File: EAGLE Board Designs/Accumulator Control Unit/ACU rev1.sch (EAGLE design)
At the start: 191 parts, among them J1 CONNECTOR-CAN_MF_T_V_, J2 CONNECTOR-8_MF_T_V_, J3 CONNECTOR-8_MF_T_V_, J4 CONNECTOR-2_MF_T_V_, J5 CONNECTOR-12_MF_T_V_, Q1 TRANSISTOR_N_MOS__PMV15ENEA, Q2 TRANSISTOR_N_MOS__PMV15ENEA, T1 TRANSFORMER_HM2112ZNLT_AIRGAP, U10 OPAMP_1_CHANNEL_OPA991, U11 LOGICGATE_AND_DCK3, U12 OPAMP_1_CHANNEL_OPA991, U13 OPAMP_1_CHANNEL_OPA991, U14 OPAMP_1_CHANNEL_OPA991, U15 LOGICGATE_AND_DCK3, U18 OPAMP_1_CHANNEL_OPA991, U19 MAX7404, U2 ADG1423, U20 OPAMP_1_CHANNEL_OPA991, U22 OPAMP_1_CHANNEL_OPA991, U25 TCAN1051HQV-Q1, U26 MAX7404, U27 OPAMP_1_CHANNEL_OPA991, U28 MAX7404, U29 OPAMP_1_CHANNEL_OPA991, U3 LM555, U30 MAX7404, U4 OPAMP_1_CHANNEL_OPA991, U5 LTC6820, U6 ADM823, U7 OPAMP_1_CHANNEL_OPA991, U8 LOGICGATE_AND_DCK3, U9 OPAMP_1_CHANNEL_OPA991

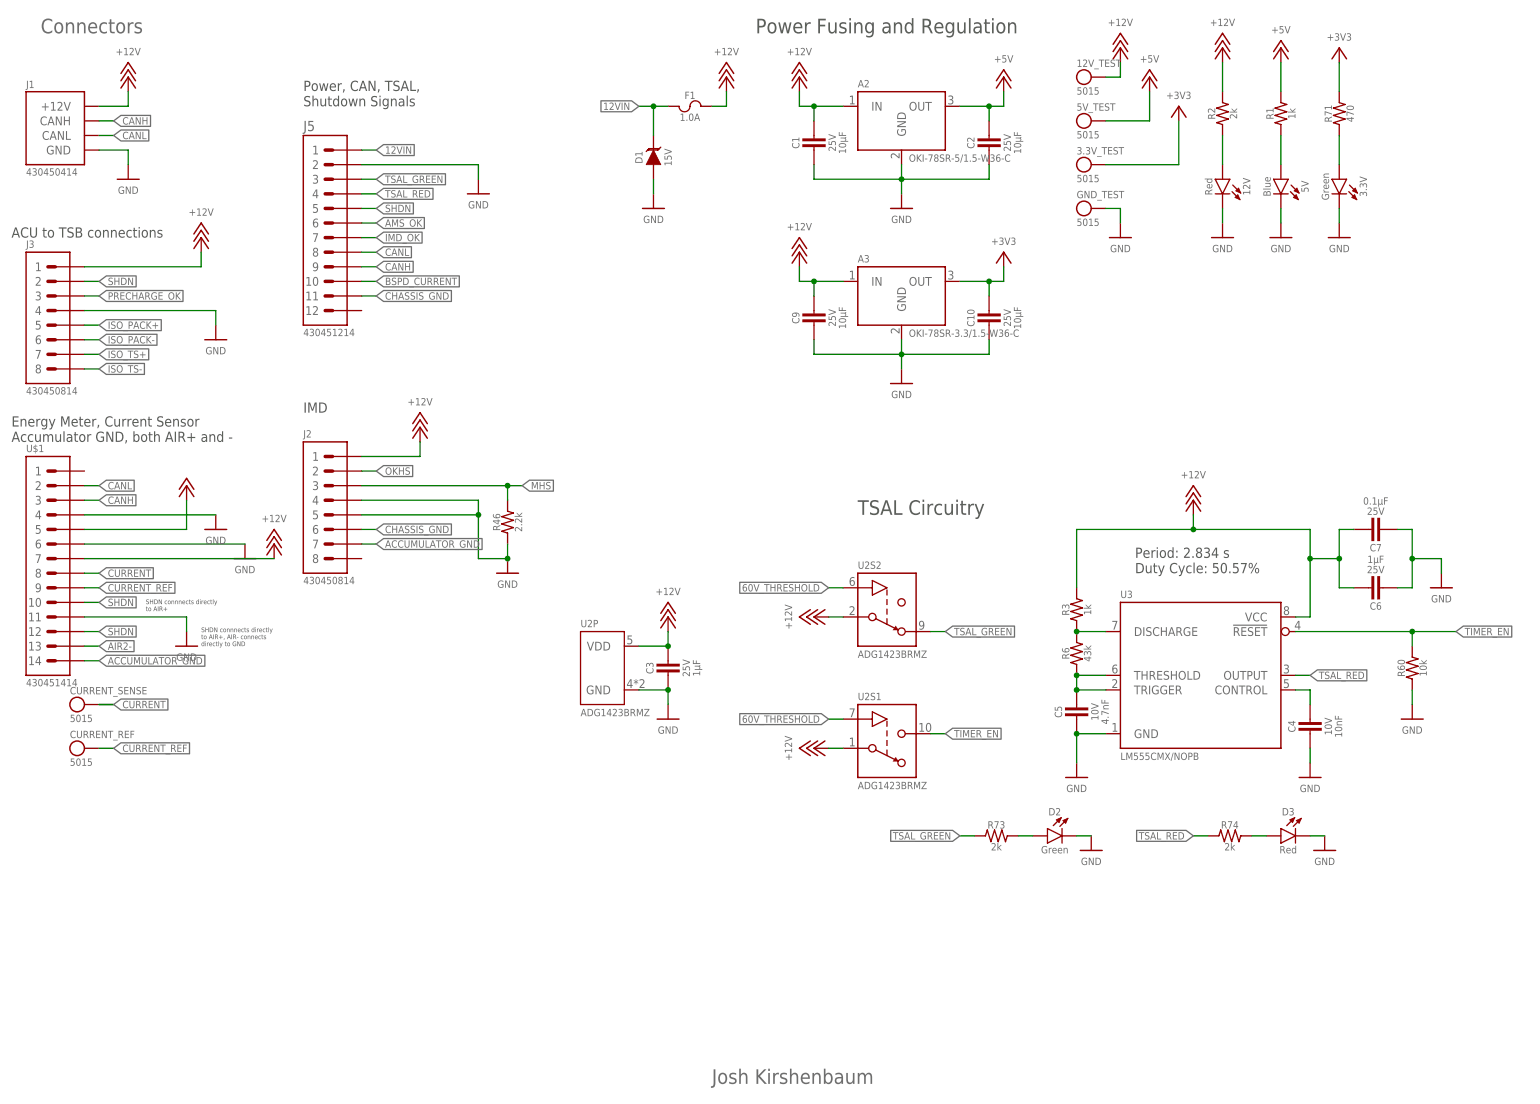
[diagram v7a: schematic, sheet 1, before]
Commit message: fix hole spacing and add some leds
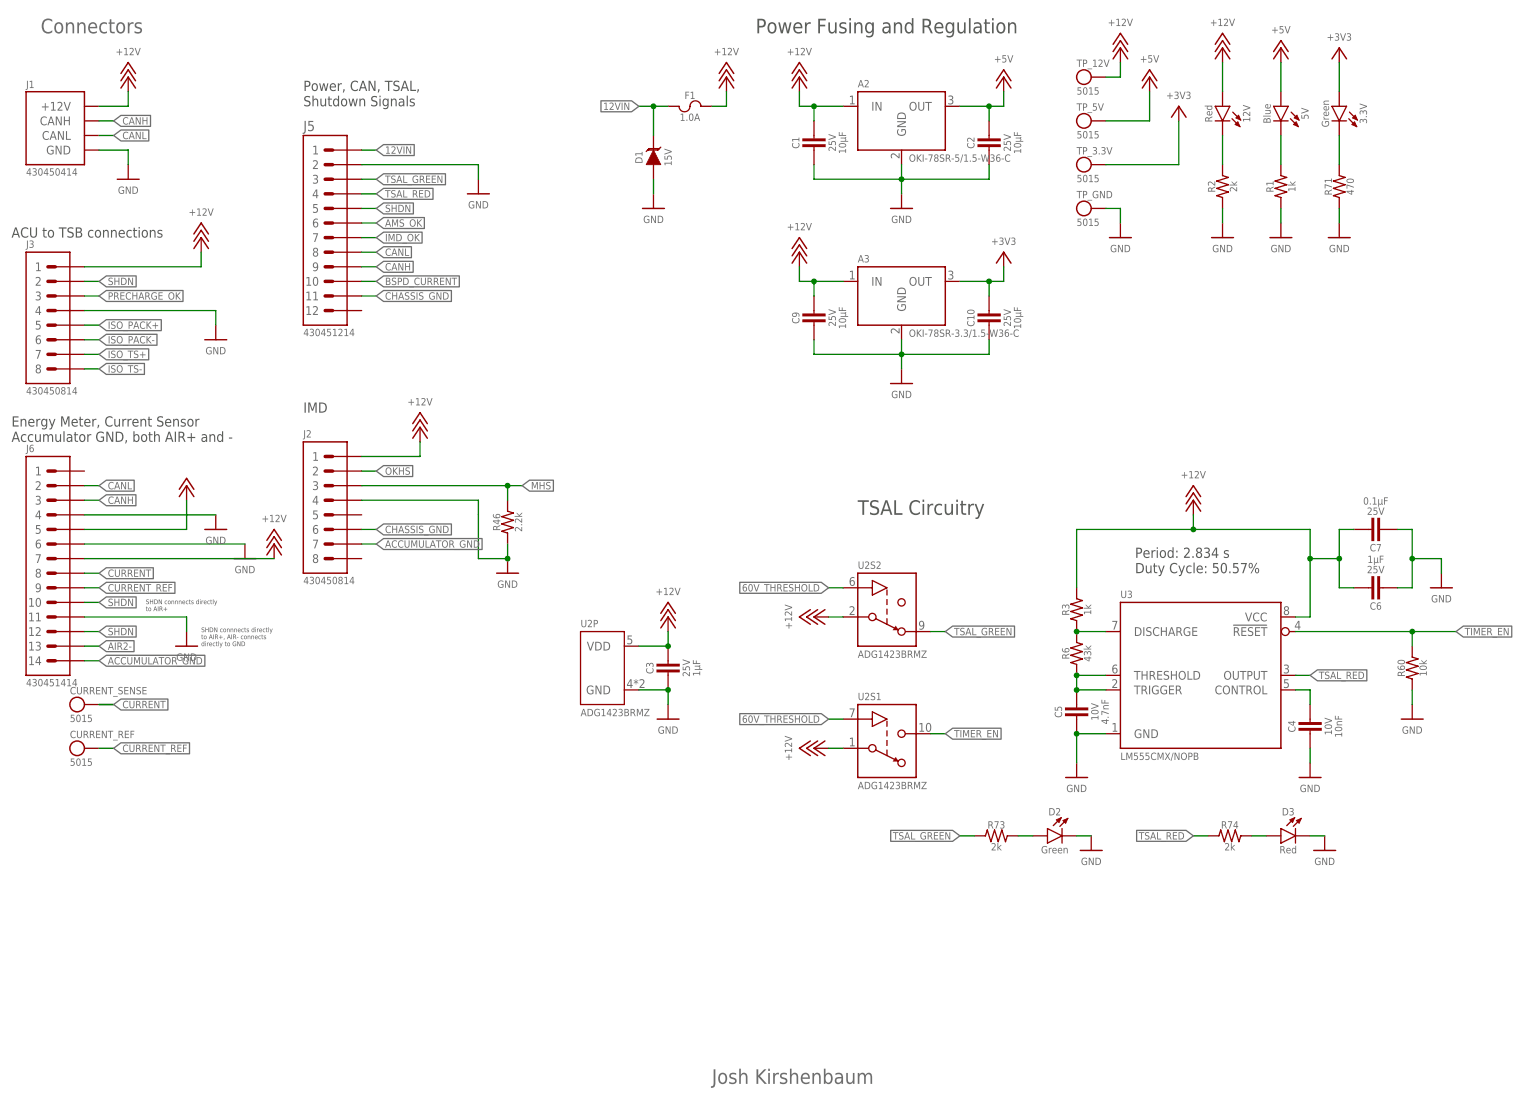
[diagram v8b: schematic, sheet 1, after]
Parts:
- added D10: LED_0603_GREEN, HyTechDevices:LED_0603_GREEN
- added D14: LED_0603_RED, HyTechDevices:LED_0603_RED
- added R75, R76: RESISTOR_0603_470, HyTechDevices - Copy:RESISTOR_0603_470
- renumbered 12V_TEST to TP_12V, 3.3V_TEST to TP_3.3V, 5V_TEST to TP_5V, AMS_OK_TEST to TP_AMS_OK, GND_TEST to TP_GND, IMD_OK_TEST to TP_IMD_OK, U$1 to J6, U$10 to U16, U$9 to U1
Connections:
- new net N$47: D10.A, R75.1
- new net N$59: D14.A, R76.1
- net +12V: now also 12V.A; no longer R2.2
- net +3V3: now also 3.3V.A; no longer R71.2
- net +5V: now also 5V.A; no longer R1.2
- net GND: now also D10.C, D14.C, R1.1, R2.1, R71.1; no longer 12V.C, 3.3V.C, 5V.C, J2.5
- net N$1: now also 3.3V.C, R71.2; no longer 12V.A, R2.1
- net N$14: now also 12V.C, R2.2; no longer 3.3V.A, R71.1
- net N$2: now also 5V.C, R1.2; no longer 5V.A, R1.1
- net TEENSY_OK: now also R76.2
- net WATCHDOG_INPUT: now also R75.2
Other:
- moved on the sheet: 12V, 3.3V, 5V, R1, R2, R71
